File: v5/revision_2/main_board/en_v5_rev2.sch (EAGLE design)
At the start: 183 parts, among them J1 M50-3142045THT, J2 M50-3142045THT, J3 53261-0271, J4 USB4105-GF-A, J5 FEMALE_HEADER_2X1, M1 SISS23DN, M2 SISS23DN, Q1 FDN302P, U1 REF3012AIDBZR, U10 CY7C1051DV33, U2 MCP73833T-AMI/MF, U3 LTC3569EUDPBF, U4 PAC1934, U5 PAC1934, U6 W25Q16JVUXIQ, U7 RP2040, U8 SPARTAN7-LX15, U9 S25FL256S, X1 12MHz, X2 32MHz, X3 100MHz

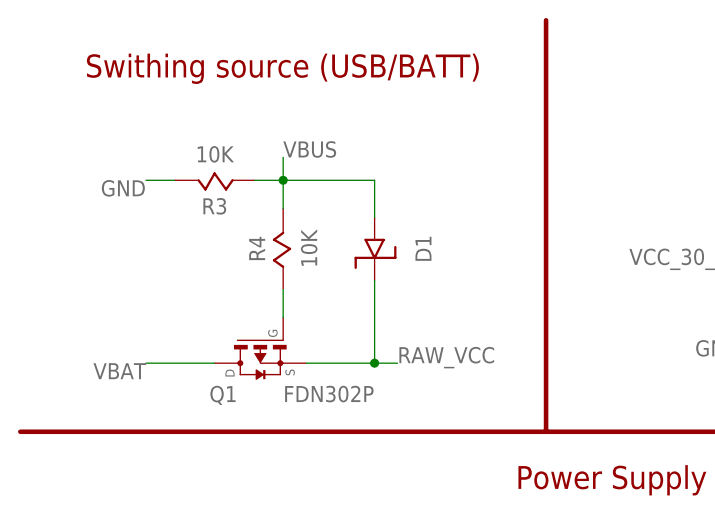
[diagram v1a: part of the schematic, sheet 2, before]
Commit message: changed a resistor value
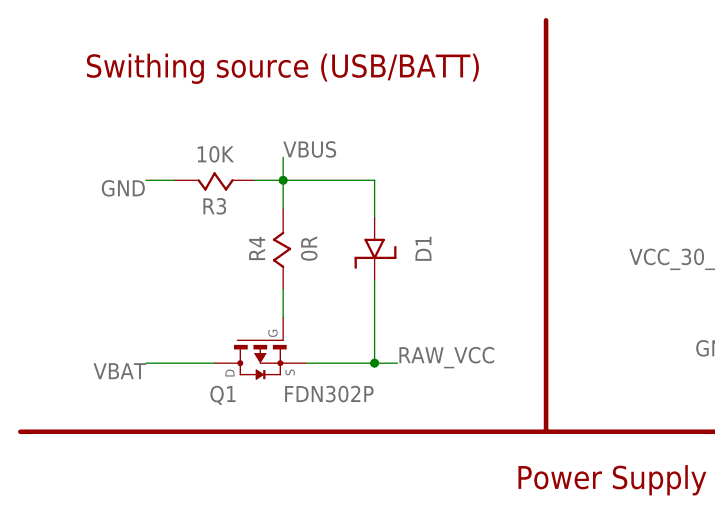
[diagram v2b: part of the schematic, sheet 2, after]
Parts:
- R4: value 10K -> 0R
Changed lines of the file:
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@@
 <drawing>
 <settings>
-<setting alwaysvectorfont="yes"/>
+<setting alwaysvectorfont="no"/>
 <setting verticaltext="up"/>
 </settings>
@@
 <attribute name="OC_NEWARK" value="unknown"/>
 </part>
-<part name="R4" library="passive" deviceset="RESISTOR" device="SMD_0402" package3d_urn="urn:adsk.eagle:package:27538107/2" value="10K">
+<part name="R4" library="passive" deviceset="RESISTOR" device="SMD_0402" package3d_urn="urn:adsk.eagle:package:27538107/2" value="0R">
 <attribute name="MF" value=""/>
 <attribute name="MPN" value=""/>

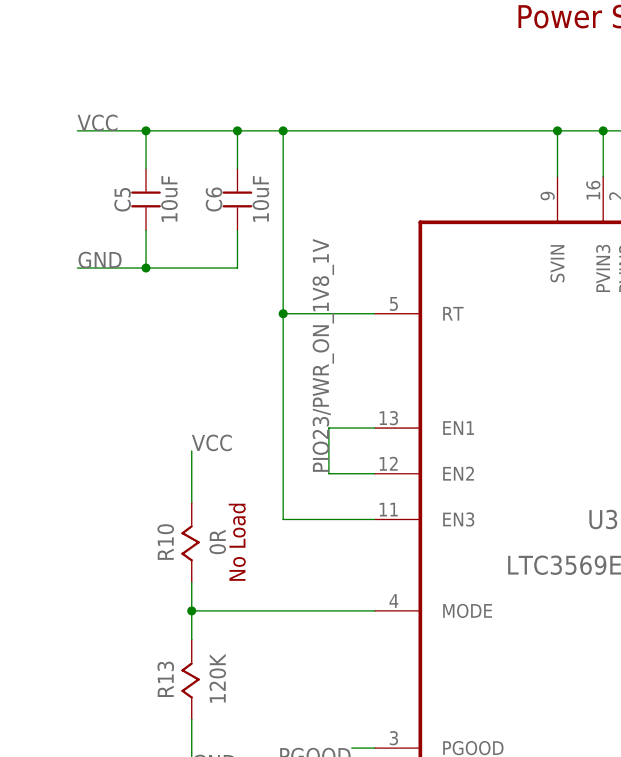
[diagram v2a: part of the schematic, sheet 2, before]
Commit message: fixed the voltage regulator
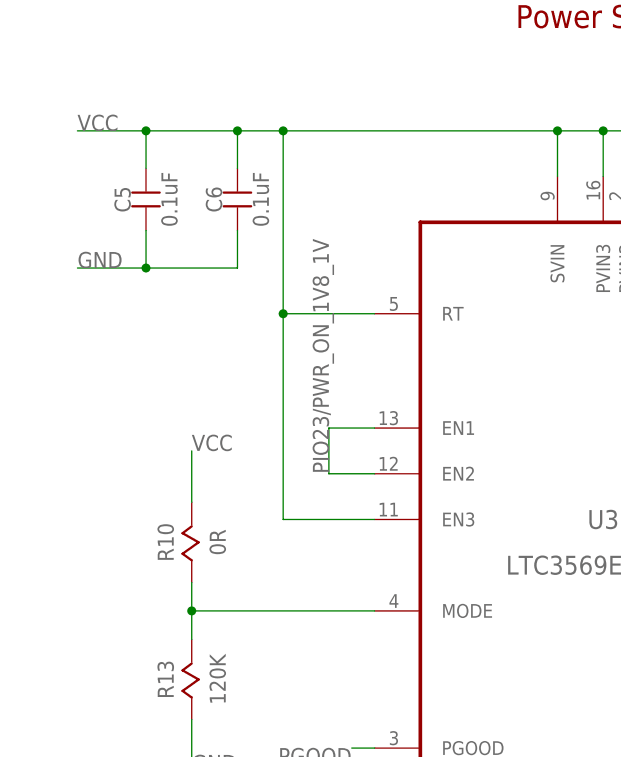
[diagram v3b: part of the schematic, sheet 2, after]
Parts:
- C1, C5, C6: value 10uF -> 0.1uF
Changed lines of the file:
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@@
 <attribute name="OC_NEWARK" value="unknown"/>
 </part>
-<part name="C1" library="passive" deviceset="CAPACITOR" device="0805" package3d_urn="urn:adsk.eagle:package:27555303/2" value="10uF">
+<part name="C1" library="passive" deviceset="CAPACITOR" device="0805" package3d_urn="urn:adsk.eagle:package:27555303/2" value="0.1uF">
 <attribute name="MF" value=""/>
 <attribute name="MPN" value=""/>
@@
 <part name="TP1" library="connectors" deviceset="TEST_POINT" device="SMD" value="TEST_POINTSMD"/>
 <part name="U3" library="power" deviceset="LTC3569EUDPBF" device=""/>
-<part name="C5" library="passive" deviceset="CAPACITOR" device="0603" package3d_urn="urn:adsk.eagle:package:27555773/1" value="10uF">
-<attribute name="MF" value=""/>
-<attribute name="MPN" value=""/>
-<attribute name="OC_NEWARK" value="unknown"/>
-</part>
-<part name="C6" library="passive" deviceset="CAPACITOR" device="0603" package3d_urn="urn:adsk.eagle:package:27555773/1" value="10uF">
+<part name="C5" library="passive" deviceset="CAPACITOR" device="0603" package3d_urn="urn:adsk.eagle:package:27555773/1" value="0.1uF">
+<attribute name="MF" value=""/>
+<attribute name="MPN" value=""/>
+<attribute name="OC_NEWARK" value="unknown"/>
+</part>
+<part name="C6" library="passive" deviceset="CAPACITOR" device="0603" package3d_urn="urn:adsk.eagle:package:27555773/1" value="0.1uF">
 <attribute name="MF" value=""/>
 <attribute name="MPN" value=""/>
@@
 <text x="99.06" y="66.04" size="1.778" layer="94">3.3uH</text>
 <text x="99.06" y="38.1" size="1.778" layer="94">2.2uH</text>
-<text x="27.94" y="66.04" size="1.778" layer="94" rot="R90" align="center">No Load</text>
 <wire x1="3.81" y1="129.54" x2="62.23" y2="129.54" width="0.508" layer="94"/>
 <wire x1="62.23" y1="129.54" x2="161.29" y2="129.54" width="0.508" layer="94"/>
